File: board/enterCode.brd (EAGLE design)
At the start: 42.8 x 54.6 mm, 14 parts, among them IC1 LM1117IMPX-3.3

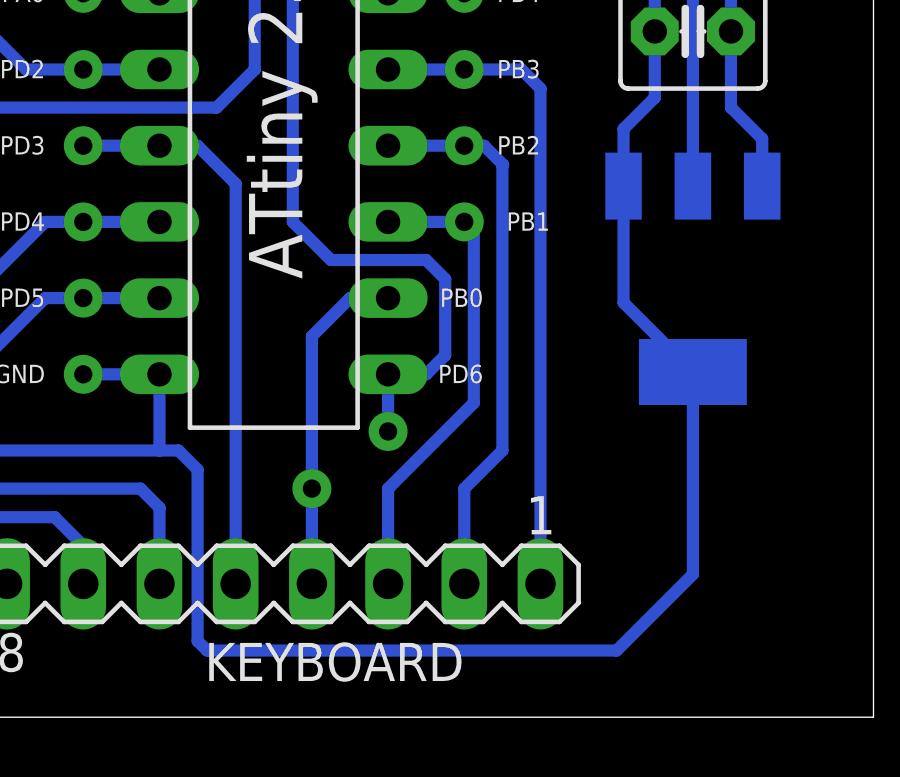
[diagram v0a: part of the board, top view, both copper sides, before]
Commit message: Correct a MAJOR error in the design: the TAB of the regulator LM1117-3.3V is not corrected to GND (as it was) *but* to 3.3V signal !!
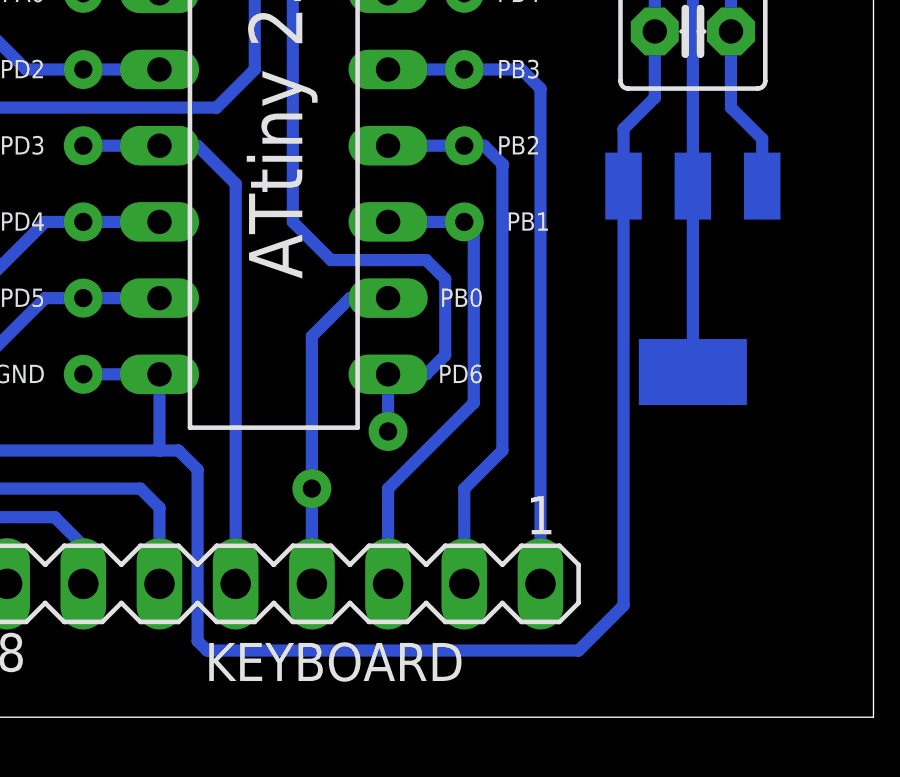
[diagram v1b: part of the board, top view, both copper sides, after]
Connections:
- net 3.3V: now also IC1.TAB
- net GND: no longer IC1.TAB
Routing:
- net 3.3V: track 38.7 -> 44.9 mm
- net GND: track 192.2 -> 189.6 mm
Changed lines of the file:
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@@
 <contactref element="IC1" pad="1"/>
 <contactref element="POWER" pad="2"/>
-<contactref element="IC1" pad="TAB"/>
 <contactref element="C3" pad="1"/>
 <contactref element="C2" pad="1"/>
@@
 <wire x1="31.75" y1="31.75" x2="29.845" y2="31.75" width="0.4064" layer="16"/>
 <wire x1="56.109" y1="32.309" x2="57.15" y2="33.35" width="0.4064" layer="16"/>
-<wire x1="56.109" y1="30.404" x2="56.109" y2="26.517" width="0.4064" layer="16"/>
-<wire x1="56.109" y1="26.517" x2="58.42" y2="24.206" width="0.4064" layer="16"/>
 <wire x1="29.21" y1="60.96" x2="29.21" y2="62.865" width="0.4064" layer="16"/>
 <wire x1="29.845" y1="31.75" x2="29.21" y2="31.115" width="0.4064" layer="16"/>
@@
 <wire x1="41.91" y1="20.955" x2="41.91" y2="15.24" width="0.4064" layer="16"/>
 <wire x1="41.91" y1="15.24" x2="42.2275" y2="14.9225" width="0.4064" layer="16"/>
-<wire x1="42.2275" y1="14.9225" x2="55.88" y2="14.9225" width="0.4064" layer="16"/>
+<wire x1="42.2275" y1="14.9225" x2="54.61" y2="14.9225" width="0.4064" layer="16"/>
 <contactref element="SV1" pad="1"/>
 <wire x1="57.15" y1="41.275" x2="57.15" y2="46.99" width="0.4064" layer="16"/>
@@
 <wire x1="42.545" y1="47.625" x2="42.545" y2="46.355" width="0.4064" layer="16"/>
 <wire x1="35.56" y1="48.26" x2="41.91" y2="48.26" width="0.4064" layer="16"/>
-<wire x1="55.88" y1="14.9225" x2="58.42" y2="17.4625" width="0.4064" layer="16"/>
-<wire x1="58.42" y1="17.4625" x2="58.42" y2="24.206" width="0.4064" layer="16"/>
 <wire x1="40.64" y1="57.15" x2="40.64" y2="54.61" width="0.4064" layer="16"/>
 <wire x1="40.64" y1="54.61" x2="40.64" y2="53.975" width="0.4064" layer="16"/>
@@
 <wire x1="27.94" y1="60.96" x2="29.21" y2="60.96" width="0.4064" layer="16"/>
 <wire x1="26.67" y1="53.34" x2="26.67" y2="59.69" width="0.4064" layer="16"/>
+<wire x1="56.109" y1="16.4215" x2="54.61" y2="14.9225" width="0.4064" layer="16"/>
+<wire x1="56.109" y1="30.404" x2="56.109" y2="16.4215" width="0.4064" layer="16"/>
 </signal>
 <signal name="VCC">
@@
 <wire x1="59.69" y1="52.07" x2="59.69" y2="46.99" width="0.4064" layer="16"/>
 <wire x1="59.69" y1="46.99" x2="59.69" y2="45.085" width="0.4064" layer="16"/>
+<contactref element="IC1" pad="TAB"/>
+<wire x1="58.42" y1="24.206" x2="58.42" y2="30.404" width="0.4064" layer="16"/>
 </signal>
 <signal name="PB4">
